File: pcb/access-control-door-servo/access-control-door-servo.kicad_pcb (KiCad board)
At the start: 2 copper layers, 52.5 x 21.4 mm, 16 parts, among them J1 Conn_01x02_Pin, U1 ATtiny404-SS

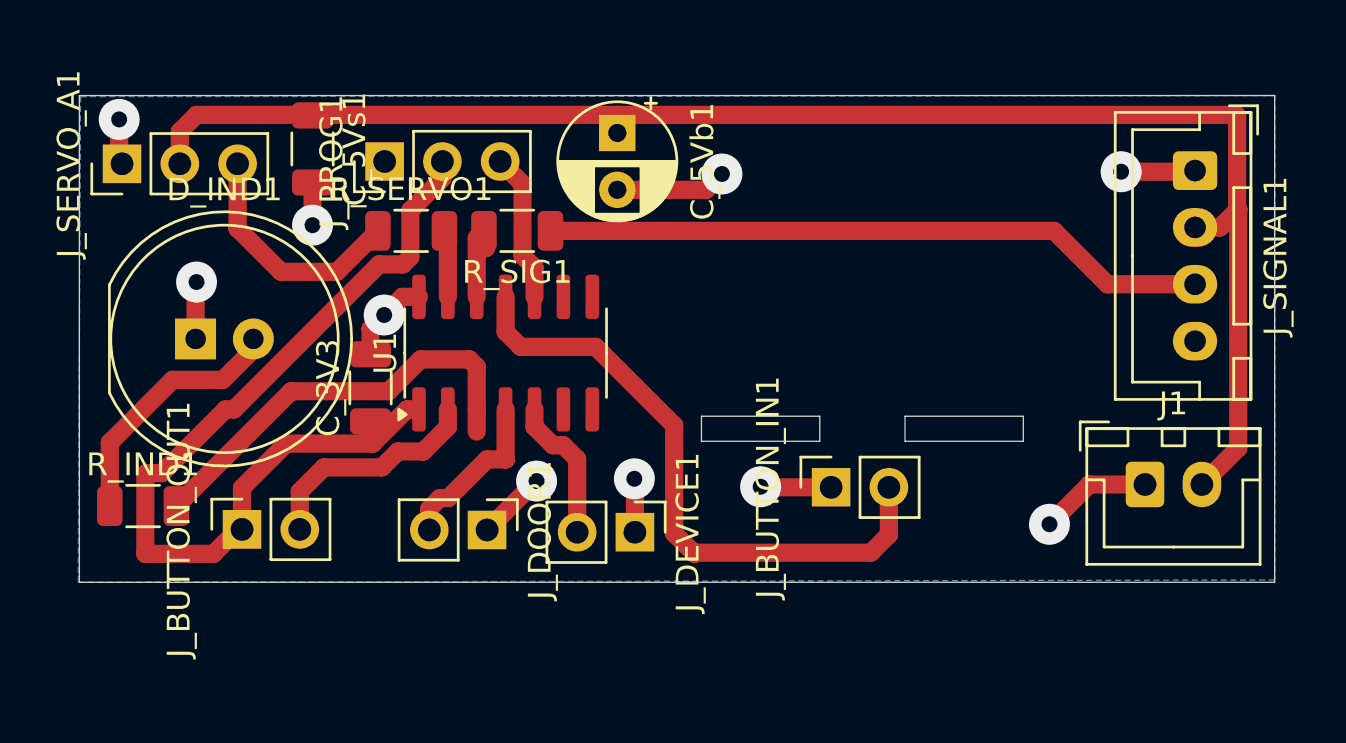
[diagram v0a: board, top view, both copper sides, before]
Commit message: Progress with work to support door servo
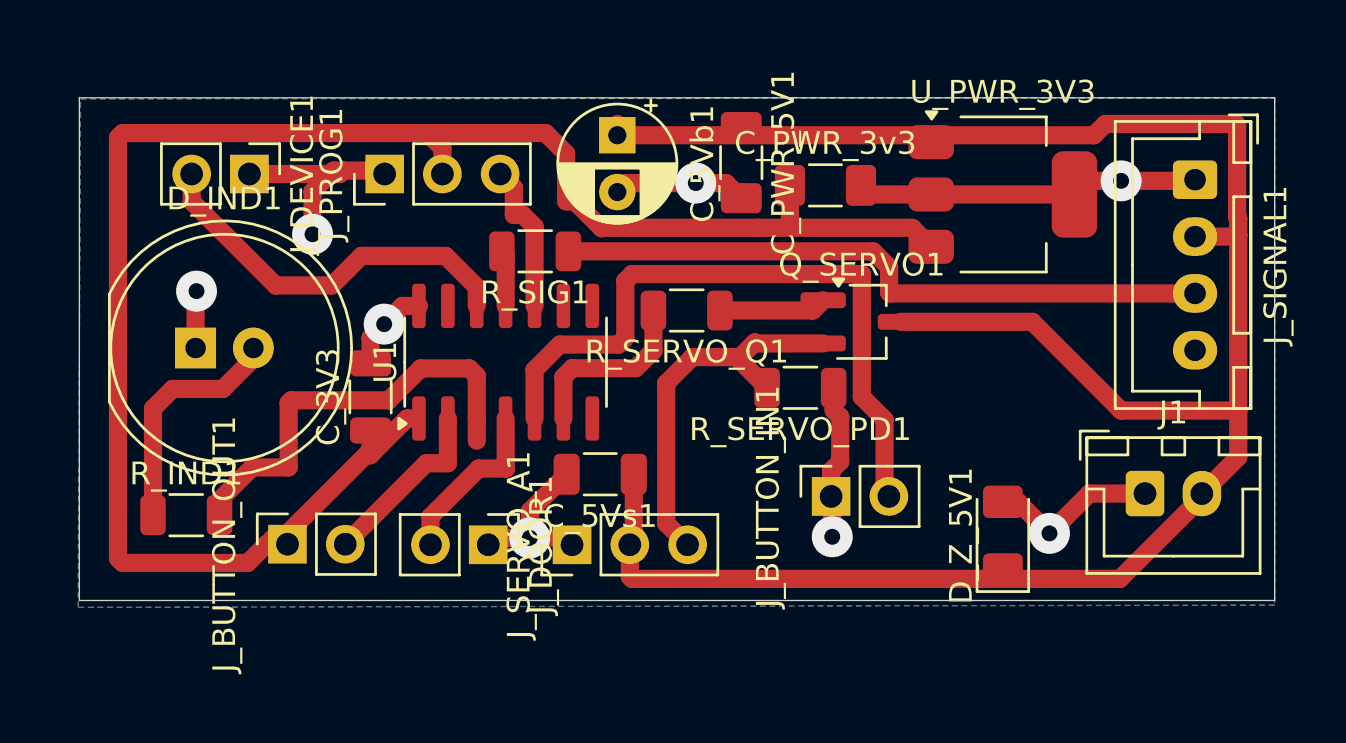
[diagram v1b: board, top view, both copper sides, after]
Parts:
- added C_PWR_3v3: 1U, Capacitor_SMD:C_1206_3216Metric_Pad1.33x1.80mm_HandSolder, F.Cu at (32.8, 3.90)
- added C_PWR_5V1: 1U, Capacitor_SMD:C_1206_3216Metric_Pad1.33x1.80mm_HandSolder, F.Cu at (29.1, 2.90)
- added D_Z_5V1: D_Zener, Diode_SMD:D_1206_3216Metric_Pad1.42x1.75mm_HandSolder, F.Cu at (40.6, 19.3)
- added Q_SERVO1: MMBT2222A, Package_TO_SOT_SMD:SOT-23W_Handsoldering, F.Cu at (34.4, 9.90)
- added R_SERVO_PD1: R, Resistor_SMD:R_1206_3216Metric, F.Cu at (31.7, 12.8)
- added U_PWR_3V3: TC1262-33, Package_TO_SOT_SMD:SOT-223-3_TabPin2, F.Cu at (40.6, 4.30)
- moved J_SERVO_A1 25.9 mm to (21.7, 19.7)
- moved J_DEVICE1 23.1 mm to (7.47, 3.40)
- moved C_5Vs1 19.1 mm to (22.9, 16.6), turned to 180 degrees
- moved R_SERVO_Q1 12.6 mm to (26.7, 9.40), turned to 180 degrees
- moved J_BUTTON_OUT1 2.10 mm to (9.15, 19.7)
- moved R_IND1 1.94 mm to (4.70, 18.4)
- moved R_SIG1 1.20 mm to (20.0, 6.80)
- moved J_DOOR1 0.65 mm to (18.0, 19.7)
- moved J_PROG1 0.55 mm to (13.4, 3.40)
- moved D_IND1 0.40 mm to (5.11, 11.1)
- moved U1 0.40 mm to (18.7, 11.7)
- moved J_SIGNAL1 0.40 mm to (49.0, 3.65)
- moved C_3V3 0.40 mm to (12.8, 13.2)
- moved J1 0.40 mm to (46.9, 17.4)
- moved J_BUTTON_IN1 0.40 mm to (33.0, 17.6)
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- renumbered R_SERVO1 to R_SERVO_Q1
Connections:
- R_SERVO_Q1 pad 1: Net-(J_SERVO_A1-Pin_3) -> Net-(Q_SERVO1-B)
- R_SERVO_Q1 pad 2: Net-(U1-PA3) -> Net-(U1-PB3)
- R_SIG1 pad 2: Net-(U1-PA2) -> Net-(U1-PA1)
- U1 pad 11: Net-(J_BUTTON_IN1-Pin_2) -> Net-(U1-PA1)
- U1 pad 12: Net-(U1-PA2) -> Net-(J_DEVICE1-Pin_2)
- U1 pad 13: Net-(U1-PA3) -> unconnected-(U1-PA3-Pad13)
- U1 pad 5: Net-(J_DEVICE1-Pin_2) -> Net-(J_BUTTON_IN1-Pin_2)
- U1 pad 6: unconnected-(U1-PB3-Pad6) -> Net-(U1-PB3)
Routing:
- net +3.3V: track 40.4 -> 79.5 mm
- net +5V: track 68.1 -> 94.9 mm
- net GND: track 31.8 -> 57.6 mm, vias 10 -> 8
- net Net-(J_DEVICE1-Pin_2): track 6.45 -> 17.2 mm
- net Net-(U1-PB3): track 0.00 -> 8.03 mm
- net Net-(J_SERVO_A1-Pin_3): track 10.6 -> 17.0 mm
- net Net-(Q_SERVO1-B): track 0.00 -> 4.72 mm
- net Net-(U1-PA2): track 3.59 -> 0.00 mm
- net Net-(U1-PA3): track 2.96 -> 0.00 mm
- net Net-(U1-PA1): track 0.00 -> 2.47 mm
- net Net-(J_BUTTON_OUT1-Pin_2): track 10.1 -> 7.95 mm
- net Net-(J_BUTTON_IN1-Pin_2): track 28.0 -> 30.0 mm
- net Net-(D_IND1-A): track 11.3 -> 10.5 mm
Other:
- board size 52.5 x 21.4 mm -> 52.5 x 22.1 mm

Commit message: Pads for TWI, space for 5v signal option
Copper on the back of relay
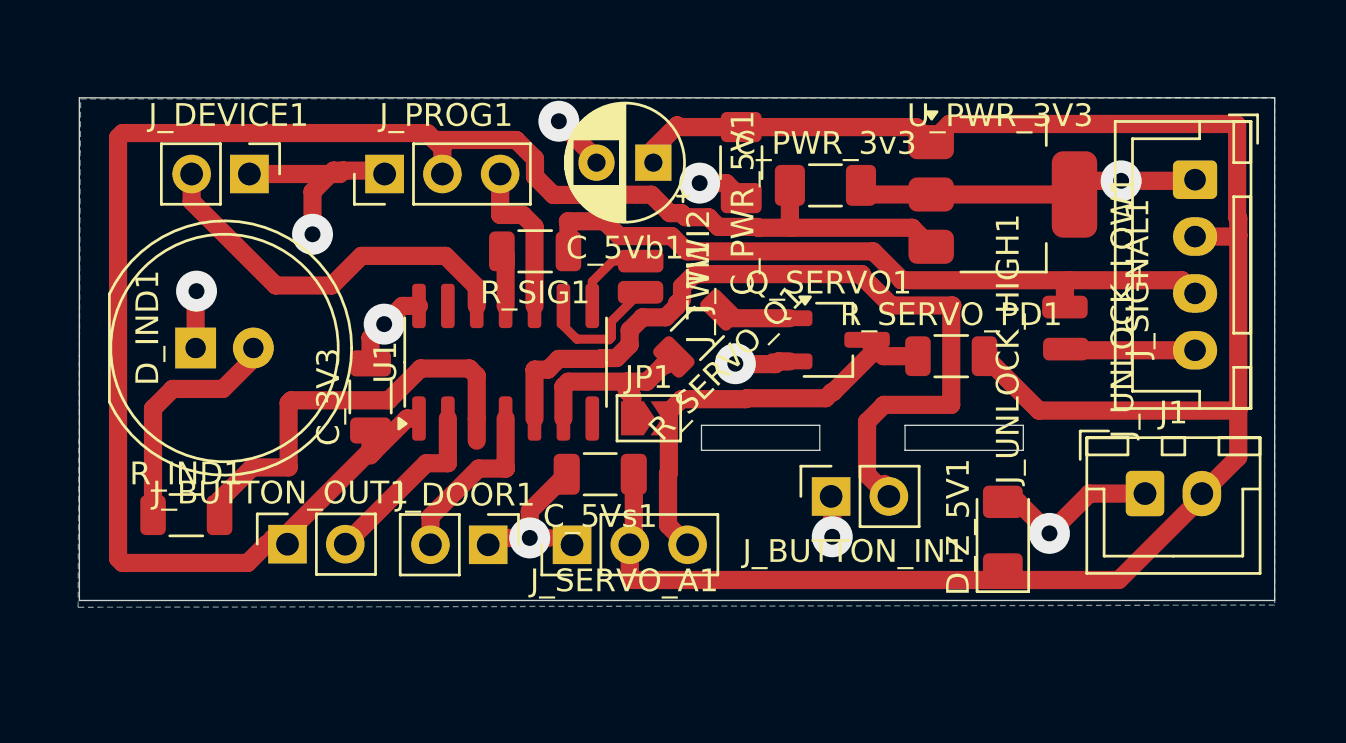
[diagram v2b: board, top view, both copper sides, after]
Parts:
- added JP1: SolderJumper_2_Open, Jumper:SolderJumper-2_P1.3mm_Open_TrianglePad1.0x1.5mm, F.Cu at (25.0, 14.1)
- added J_TWI1: Conn_01x01_Pin, Connector_Wire:SolderWirePad_1x01_SMD_1x2mm, F.Cu at (24.7, 8.60)
- added J_TWI2: Conn_01x01_Pin, Connector_Wire:SolderWirePad_1x01_SMD_1x2mm, F.Cu at (24.7, 7.23)
- added J_UNLOCK_HIGH1: Conn_01x01_Pin, Connector_Wire:SolderWirePad_1x01_SMD_1x2mm, F.Cu at (43.4, 11.1)
- added J_UNLOCK_LOW1: Conn_01x01_Pin, Connector_Wire:SolderWirePad_1x01_SMD_1x2mm, F.Cu at (43.3, 9.25)
- moved R_SERVO_PD1 6.77 mm to (38.3, 11.4), turned to 0 degrees
- moved C_5Vb1 1.99 mm to (25.2, 2.90), turned to 180 degrees
- moved Q_SERVO1 1.67 mm to (32.9, 10.7)
- moved R_SERVO_Q1 1.11 mm to (27.2, 10.4), turned to -135 degrees
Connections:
- J_SERVO_A1 pad 3: Net-(J_SERVO_A1-Pin_3) -> Net-(JP1-B)
- J_SIGNAL1 pad 4: unconnected-(J_SIGNAL1-Pin_4-Pad4) -> Net-(J_SIGNAL1-Pin_4)
- Q_SERVO1 pad 2: Net-(J_SERVO_A1-Pin_3) -> GND
- Q_SERVO1 pad 3: +5V -> Net-(JP1-B)
- R_SERVO_PD1 pad 1: GND -> Net-(JP1-B)
- R_SERVO_PD1 pad 2: Net-(J_SERVO_A1-Pin_3) -> +5V
- U1 pad 8: unconnected-(U1-PB1-Pad8) -> Net-(J_TWI2-Pin_1)
- U1 pad 9: unconnected-(U1-PB0-Pad9) -> Net-(J_TWI1-Pin_1)
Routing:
- net Net-(JP1-B): track 0.00 -> 19.0 mm
- net Net-(J_SERVO_A1-Pin_3): track 17.0 -> 0.00 mm
- net Net-(J_BUTTON_IN1-Pin_2): track 30.0 -> 36.4 mm
- net Net-(J_TWI1-Pin_1): track 0.00 -> 5.79 mm
- net Net-(J_SIGNAL1-Pin_4): track 0.00 -> 5.70 mm
- net +5V: track 94.9 -> 89.7 mm
- net Net-(J_TWI2-Pin_1): track 0.00 -> 3.57 mm
- net GND: track 57.6 -> 54.1 mm, vias 8 -> 10
- net Net-(J_SIGNAL1-Pin_3): track 29.0 -> 31.5 mm
- net Net-(Q_SERVO1-B): track 4.72 -> 3.18 mm
- net +3.3V: track 79.5 -> 78.2 mm
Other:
- outline, holes or cut-outs redrawn
